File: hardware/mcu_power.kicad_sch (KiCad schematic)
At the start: 81 parts, among them J3 OLED, Q4 IRLML2244, Q5 MMBT3904, SW1 Button Up, SW2 Button Down, SW3 Reset, SW4 Button Escape, SW5 Button Left, SW6 Button Enter, SW7 Button Right, SW8 Button Power, U10 STM32F405RGTx, U11 TPS7A2033, U2 TP6841S6, Y1 8 MHz

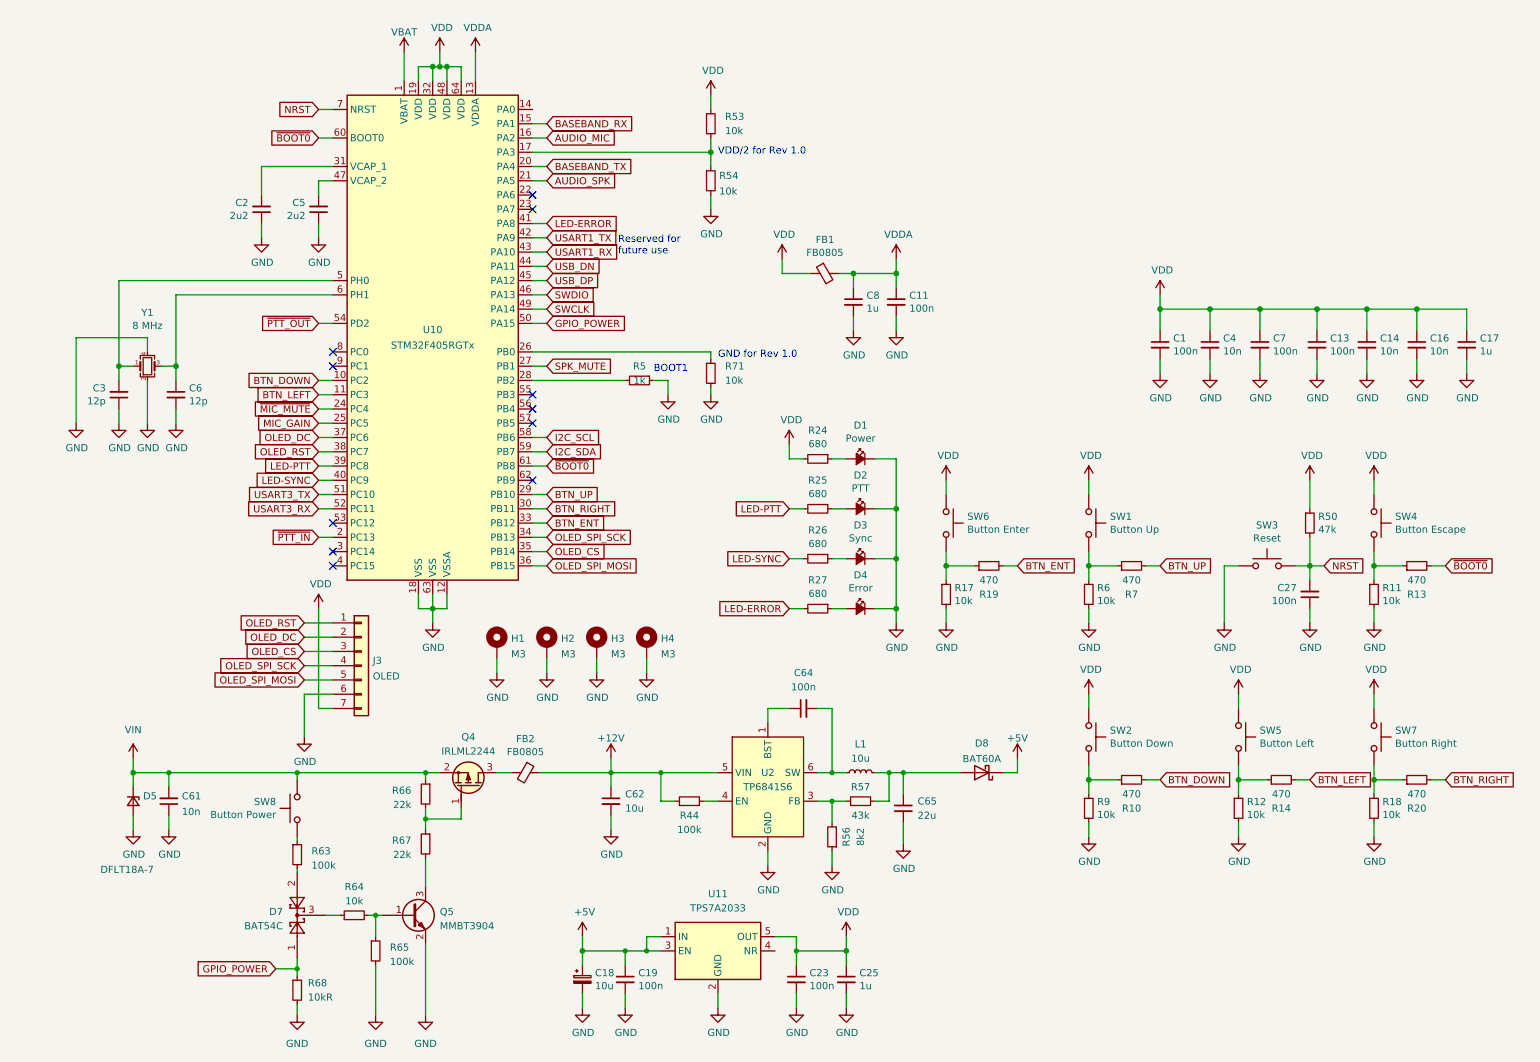
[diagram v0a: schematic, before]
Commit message: Reworked schematic
Rearranged disposition and renumbered components
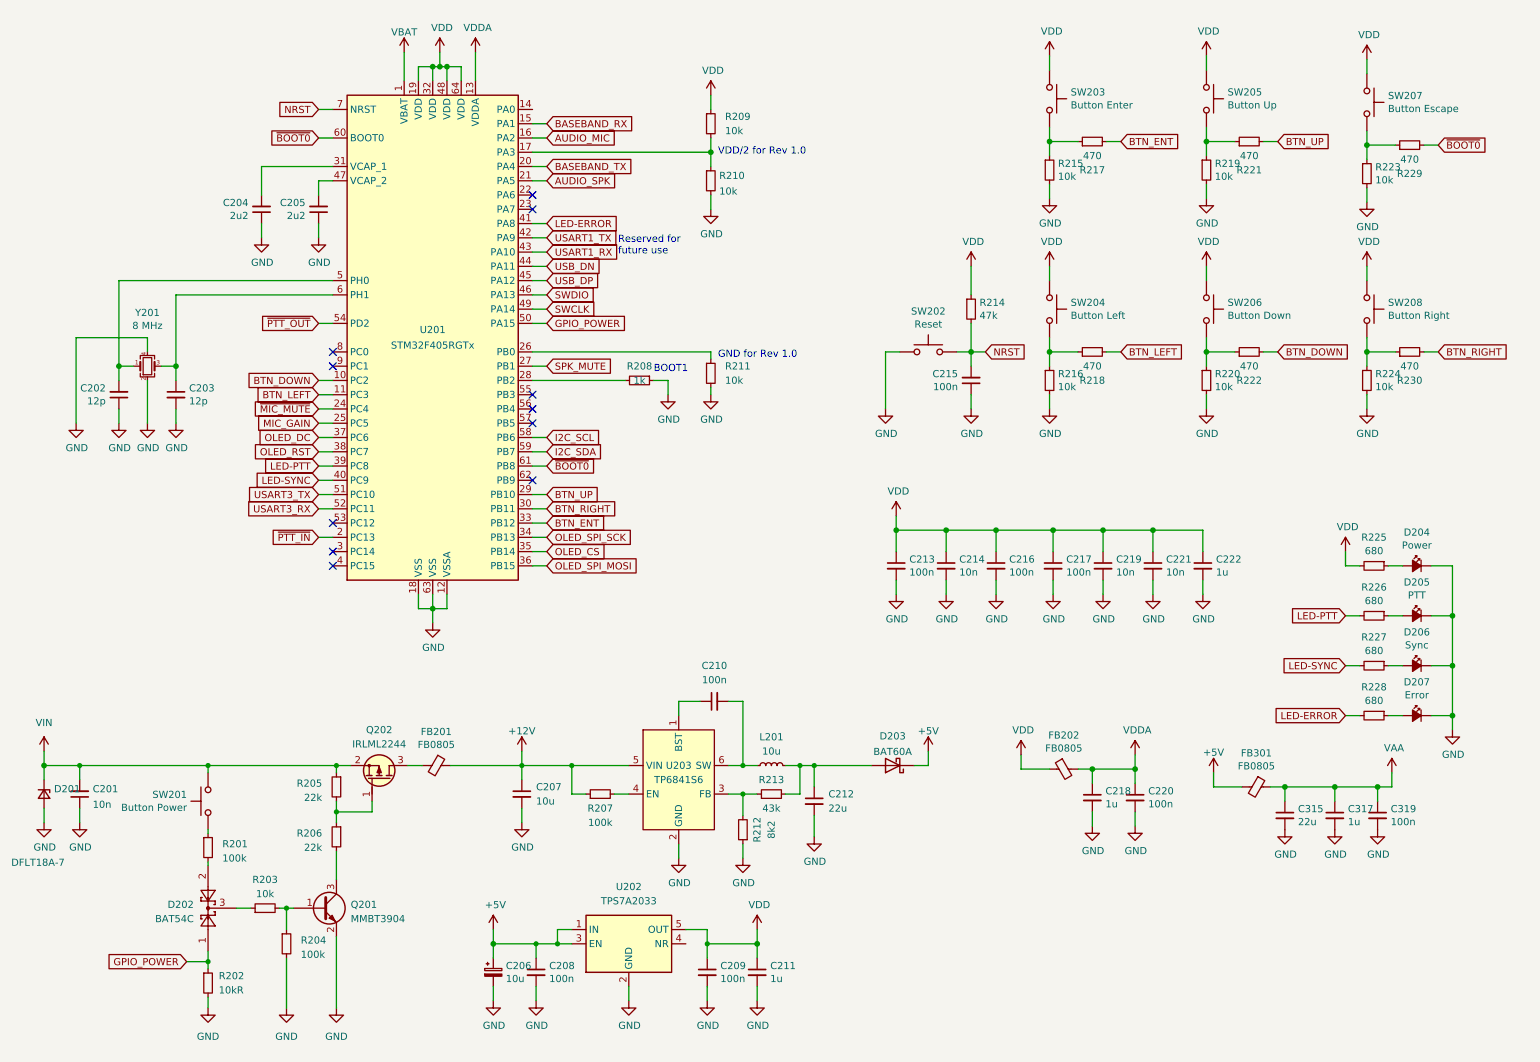
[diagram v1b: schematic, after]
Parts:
- removed H1, H2, H3, H4: M3, MountingHole:MountingHole_2.7mm_M2.5_DIN965_Pad, symbol Mechanical:MountingHole_Pad
- removed J3: OLED, Connector_PinHeader_2.54mm:PinHeader_1x07_P2.54mm_Vertical, symbol Connector_Generic:Conn_01x07
- added C315: 22u, pkl_dipol:C_0603, symbol pkl_device:pkl_C_Small
- added C317: 1u, pkl_dipol:C_0603, symbol pkl_device:pkl_C_Small
- added C319: 100n, pkl_dipol:C_0603, symbol pkl_device:pkl_C_Small
- added FB301: FB0805, pkl_dipol:L_0805, symbol Device:Ferrite_Bead_Small
- renumbered C61 to C201, C3 to C202, C6 to C203, C2 to C204, C5 to C205, C18 to C206, C62 to C207, C19 to C208, C23 to C209, C64 to C210, C25 to C211, C65 to C212, C1 to C213, C4 to C214, C27 to C215, C7 to C216, C13 to C217, C8 to C218, C14 to C219, C11 to C220, C16 to C221, C17 to C222, D5 to D201, D7 to D202, D8 to D203, D1 to D204, D2 to D205, D3 to D206, D4 to D207, FB2 to FB201, FB1 to FB202, L1 to L201, Q5 to Q201, Q4 to Q202, R63 to R201, R68 to R202, R64 to R203, R65 to R204, R66 to R205, R67 to R206, R44 to R207, R5 to R208, R53 to R209, R54 to R210, R71 to R211, R56 to R212, R57 to R213, R50 to R214, R17 to R215, R12 to R216, R19 to R217, R14 to R218, R6 to R219, R9 to R220, R7 to R221, R10 to R222, R11 to R223, R18 to R224, R24 to R225, R25 to R226, R26 to R227, R27 to R228, R13 to R229, R20 to R230, SW8 to SW201, SW3 to SW202, SW6 to SW203, SW5 to SW204, SW1 to SW205, SW2 to SW206, SW4 to SW207, SW7 to SW208, U10 to U201, U11 to U202, U2 to U203, Y1 to Y201
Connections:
- net +5V: now also FB301.2
- net GND: now also C315.2, C317.2, C319.2
- new net VAA: C315.1, C317.1, C319.1, FB301.1
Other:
- moved on the sheet: C201, C206, C207, C208, C209, C210, C211, C212, C213, C214, C215, C216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

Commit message: Updated power supply filters
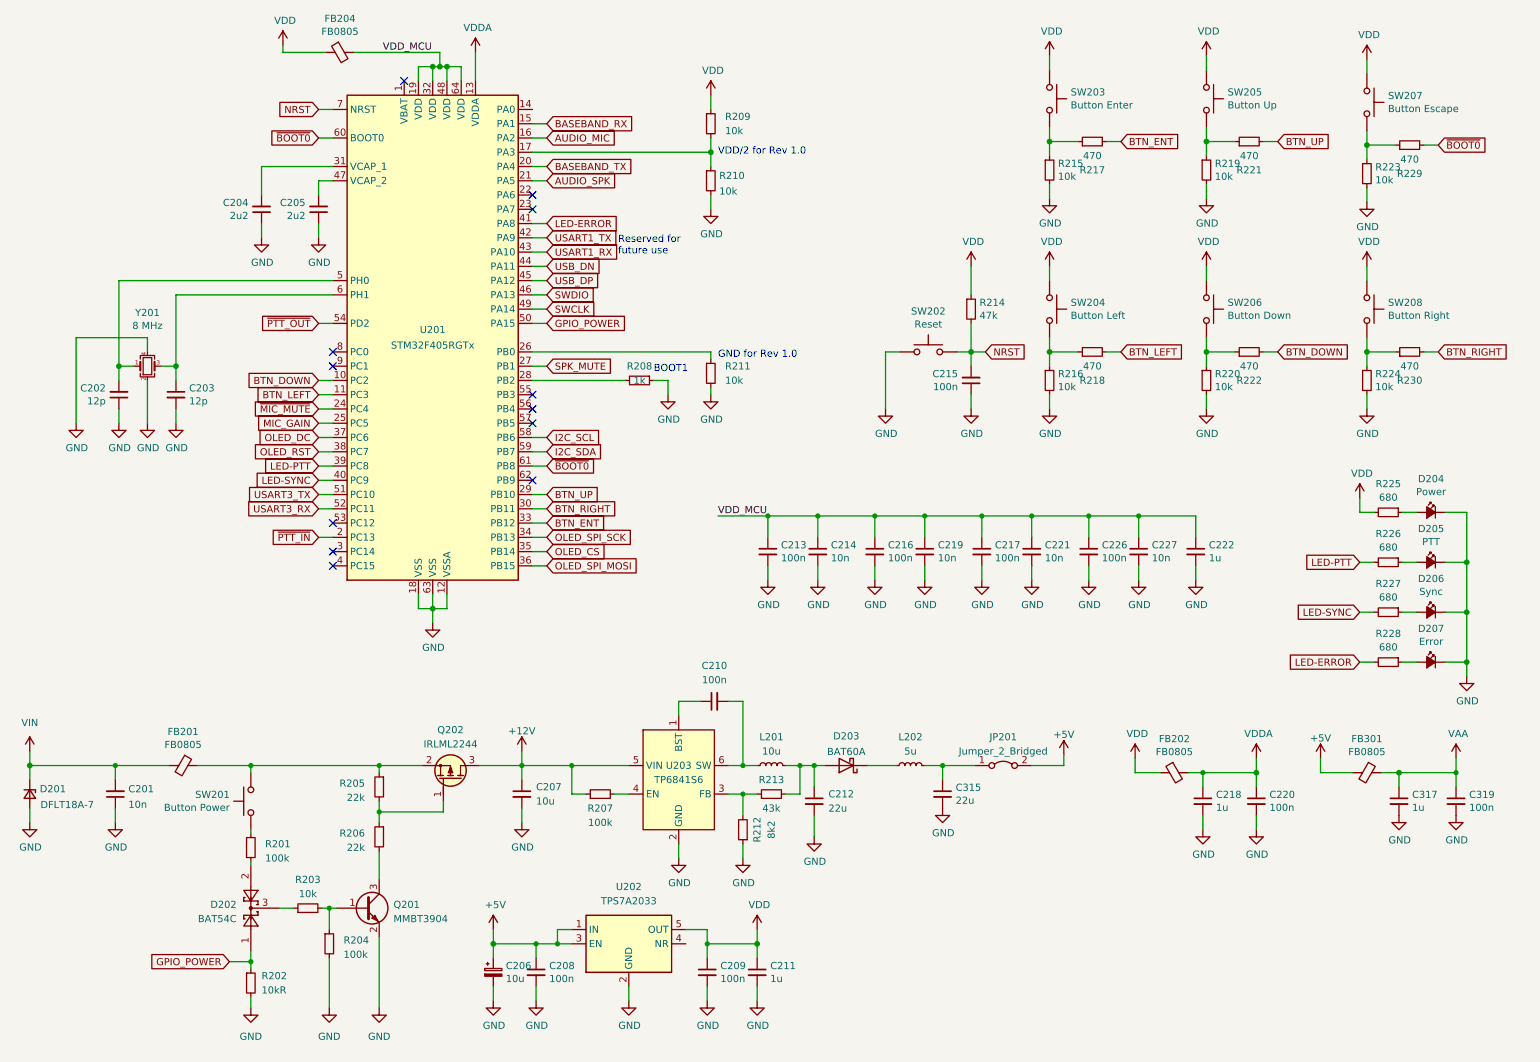
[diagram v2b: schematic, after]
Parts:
- added C226: 100n, pkl_dipol:C_0603, symbol pkl_device:pkl_C_Small
- added C227: 10n, pkl_dipol:C_0603, symbol pkl_device:pkl_C_Small
- added FB204: FB0805, pkl_dipol:L_0805, symbol Device:Ferrite_Bead_Small
- added JP201: Jumper_2_Bridged, Connector_PinHeader_2.54mm:PinHeader_1x02_P2.54mm_Vertical, symbol Jumper:Jumper_2_Bridged
- added L202: 5u, pkl_dipol:L_0805, symbol pkl_device:pkl_L_Small
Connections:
- net +12V: now also Q202.3 (D); no longer FB201.1
- net +5V: now also JP201.2 (B); no longer D203.1 (K)
- net GND: now also C226.2, C227.2
- net VAA: no longer C315.1
- net VDD: now also FB204.1; no longer C213.1, C214.1, C216.1, C217.1, C219.1, C221.1, C222.1, U201.19 (VDD), U201.32 (VDD), U201.48 (VDD), U201.64 (VDD)
- net VIN: now also FB201.2; no longer Q202.2 (S), R205.1, SW201.1
- net VBAT: no longer names the net of U201.1 (VBAT)
- new net: C315.1, JP201.1 (A), L202.1
- new net: FB201.1, Q202.2 (S), R205.1, SW201.1
- new net: D203.1 (K), L202.2
- new net VDD_MCU: C213.1, C214.1, C216.1, C217.1, C219.1, C221.1, C222.1, C226.1, C227.1, FB204.2, U201.19 (VDD), U201.32 (VDD), U201.48 (VDD), U201.64 (VDD)
- no-connect marks 11 -> 12
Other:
- moved on the sheet: C201, C213, C214, C216, C217, C218, C220, C221, C222, C315, C317, C319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

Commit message: PCB Layout [WIP]
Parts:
- removed D201: DFLT18A-7, Diode_SMD:D_SOD-128, symbol Device:D_Zener_Small
- added D201: DFLT18A-7, Diode_SMD:D_SOD-128, symbol Device:D_TVS
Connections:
- net GND: now also D201.2 (A2)
- net VIN: now also D201.1 (A1)
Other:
- moved on the sheet: C201
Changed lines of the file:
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@@
     (stroke (width 0) (type default))
   )
-  (wire (pts (xy 34.925 153.67) (xy 34.925 156.21))
+  (wire (pts (xy 34.925 154.94) (xy 34.925 158.115))
     (stroke (width 0) (type solid))
   )
@@
     (stroke (width 0) (type solid))
   )
+  (wire (pts (xy 19.685 156.21) (xy 19.685 158.115))
+    (stroke (width 0) (type default))
+  )
   (wire (pts (xy 259.08 118.745) (xy 256.54 118.745))
     (stroke (width 0) (type solid))
@@
     (stroke (width 0) (type solid))
   )
-  (wire (pts (xy 19.685 153.67) (xy 19.685 156.21))
-    (stroke (width 0) (type solid))
-  )
   (wire (pts (xy 93.98 24.13) (xy 93.98 21.59))
     (stroke (width 0) (type solid))
@@
     (stroke (width 0) (type solid))
   )
-  (wire (pts (xy 34.925 146.05) (xy 34.925 148.59))
+  (wire (pts (xy 34.925 146.05) (xy 34.925 149.86))
     (stroke (width 0) (type solid))
   )
@@
     )
   )
-  (symbol (lib_id "power:GND") (at 19.685 156.21 0) (unit 1)
+  (symbol (lib_id "power:GND") (at 19.685 158.115 0) (unit 1)
     (in_bom yes) (on_board yes) (dnp no)
-    (property "Reference" "#PWR0202" (at 19.685 162.56 0)
+    (property "Reference" "#PWR0202" (at 19.685 164.465 0)
       (effects (font (size 1.27 1.27)) hide)
     )
-    (property "Value" "GND" (at 19.812 160.6042 0)
+    (property "Value" "GND" (at 19.812 162.5092 0)
       (effects (font (size 1.27 1.27)))
     )
-    (property "Footprint" "" (at 19.685 156.21 0)
+    (property "Footprint" "" (at 19.685 158.115 0)
       (effects (font (size 1.27 1.27)) hide)
     )
-    (property "Datasheet" "" (at 19.685 156.21 0)
+    (property "Datasheet" "" (at 19.685 158.115 0)
       (effects (font (size 1.27 1.27)) hide)
     )
@@
     )
   )
+  (symbol (lib_id "Device:D_TVS") (at 19.685 152.4 270) (unit 1)
+    (in_bom yes) (on_board yes) (dnp no)
+    (property "Reference" "D201" (at 21.59 151.13 90)
+      (effects (font (size 1.27 1.27)) (justify left))
+    )
+    (property "Value" "DFLT18A-7 " (at 21.59 153.67 90)
+      (effects (font (size 1.27 1.27)) (justify left))
+    )
+    (property "Footprint" "Diode_SMD:D_SOD-128" (at 19.685 152.4 0)
+      (effects (font (size 1.27 1.27)) hide)
+    )
+    (property "Datasheet" "~" (at 19.685 152.4 0)
+      (effects (font (size 1.27 1.27)) hide)
+    )
+    (property "LCSC Part #" "C2909295" (at 19.685 152.4 0)
+      (effects (font (size 1.27 1.27)) hide)
+    )
+    (property "MPN" "DFLT18A-7" (at 19.685 152.4 0)
+      (effects (font (size 1.27 1.27)) hide)
+    )
+    (pin "1")
+    (pin "2")
+    (instances
+      (project "M17-SmartMic"
+        (path "/59592280-3207-432b-a891-cd517ec5cf12/00000000-0000-0000-0000-0000612c95ef"
+          (reference "D201") (unit 1)
+        )
+      )
+    )
+  )
   (symbol (lib_id "power:+5V") (at 249.555 144.78 0) (unit 1)
     (in_bom yes) (on_board yes) (dnp no) (fields_autoplaced)
@@
     )
   )
-  (symbol (lib_id "Device:D_Zener_Small") (at 19.685 151.13 270) (unit 1)
-    (in_bom no) (on_board yes) (dnp no)
-    (property "Reference" "D201" (at 21.4631 150.2215 90)
-      (effects (font (size 1.27 1.27)) (justify left))
-    )
-    (property "Value" "DFLT18A-7 " (at 21.59 153.035 90)
-      (effects (font (size 1.27 1.27)) (justify left))
-    )
-    (property "Footprint" "Diode_SMD:D_SOD-128" (at 19.685 151.13 90)
-      (effects (font (size 1.27 1.27)) hide)
-    )
-    (property "Datasheet" "~" (at 19.685 151.13 90)
-      (effects (font (size 1.27 1.27)) hide)
-    )
-    (property "MPN" "DFLT18A-7" (at 19.685 151.13 0)
-      (effects (font (size 1.27 1.27)) hide)
-    )
-    (property "LCSC Part #" "C2909295" (at 19.685 151.13 0)
-      (effects (font (size 1.27 1.27)) hide)
-    )
-    (pin "1")
-    (pin "2")
-    (instances
-      (project "M17-SmartMic"
-        (path "/59592280-3207-432b-a891-cd517ec5cf12/00000000-0000-0000-0000-0000612c95ef"
-          (reference "D201") (unit 1)
-        )
-      )
-    )
-  )
   (symbol (lib_id "pkl_power:VIN") (at 19.685 143.51 0) (unit 1)
     (in_bom yes) (on_board yes) (dnp no) (fields_autoplaced)
@@
     )
   )
-  (symbol (lib_id "pkl_device:pkl_C_Small") (at 34.925 151.13 180) (unit 1)
+  (symbol (lib_id "pkl_device:pkl_C_Small") (at 34.925 152.4 180) (unit 1)
     (in_bom yes) (on_board yes) (dnp no) (fields_autoplaced)
-    (property "Reference" "C201" (at 37.2492 150.2215 0)
+    (property "Reference" "C201" (at 37.2492 151.4915 0)
       (effects (font (size 1.27 1.27)) (justify right))
     )
-    (property "Value" "10n" (at 37.2492 152.9966 0)
+    (property "Value" "10n" (at 37.2492 154.2666 0)
       (effects (font (size 1.27 1.27)) (justify right))
     )
-    (property "Footprint" "pkl_dipol:C_0603" (at 34.925 151.13 0)
+    (property "Footprint" "pkl_dipol:C_0603" (at 34.925 152.4 0)
       (effects (font (size 1.524 1.524)) hide)
     )
-    (property "Datasheet" "" (at 34.925 151.13 0)
+    (property "Datasheet" "" (at 34.925 152.4 0)
       (effects (font (size 1.524 1.524)))
     )
-    (property "MPN" "Generic C/10nF/C0G/25V/0603" (at 34.925 151.13 0)
+    (property "MPN" "Generic C/10nF/C0G/25V/0603" (at 34.925 152.4 0)
       (effects (font (size 1.27 1.27)) hide)
     )
@@
     )
   )
-  (symbol (lib_id "power:GND") (at 34.925 156.21 0) (unit 1)
+  (symbol (lib_id "power:GND") (at 34.925 158.115 0) (unit 1)
     (in_bom yes) (on_board yes) (dnp no)
-    (property "Reference" "#PWR0204" (at 34.925 162.56 0)
+    (property "Reference" "#PWR0204" (at 34.925 164.465 0)
       (effects (font (size 1.27 1.27)) hide)
     )
-    (property "Value" "GND" (at 35.052 160.6042 0)
+    (property "Value" "GND" (at 35.052 162.5092 0)
       (effects (font (size 1.27 1.27)))
     )
-    (property "Footprint" "" (at 34.925 156.21 0)
+    (property "Footprint" "" (at 34.925 158.115 0)
       (effects (font (size 1.27 1.27)) hide)
     )
-    (property "Datasheet" "" (at 34.925 156.21 0)
+    (property "Datasheet" "" (at 34.925 158.115 0)
       (effects (font (size 1.27 1.27)) hide)
     )
